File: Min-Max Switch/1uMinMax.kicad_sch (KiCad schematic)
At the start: 47 parts, among them J1 PJ301M12, J2 PJ301M12, J3 PJ301M12, J4 PJ301M12, J5 PJ301M12, J6 PJ301M12, J7 PJ301M12, J8 PJ301M12, P1 CONN_01X03, U1 TL074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

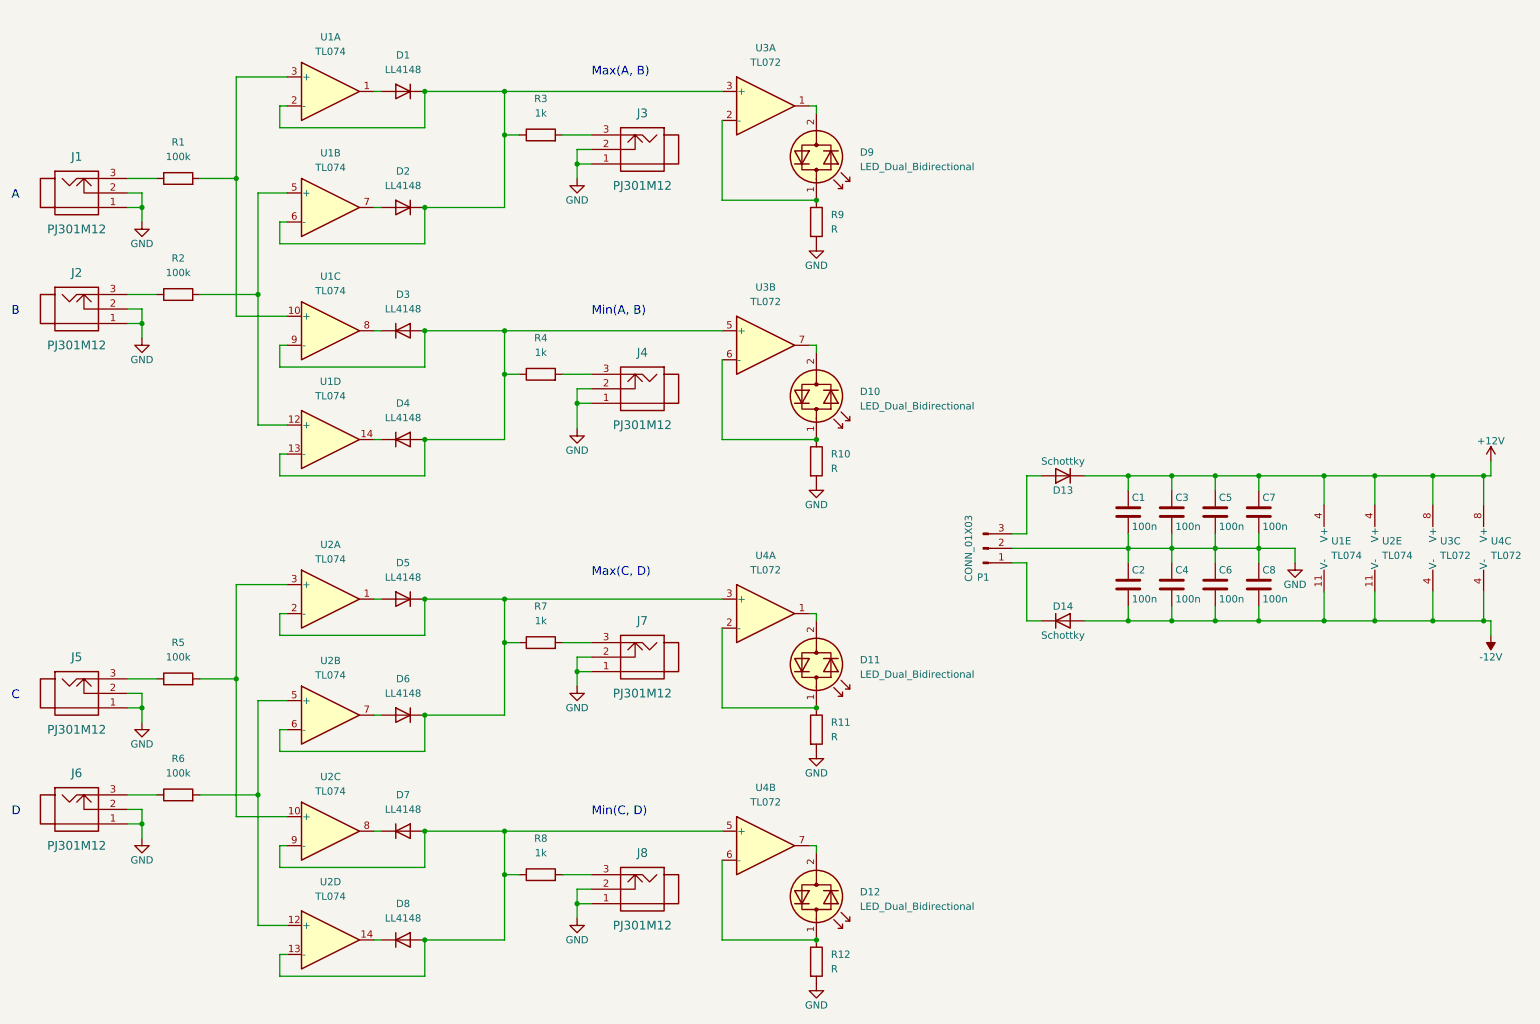
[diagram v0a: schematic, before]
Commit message: Updated sub-dom switch circuit. It now clones a section of the Mutable Instruments Kinks circuit
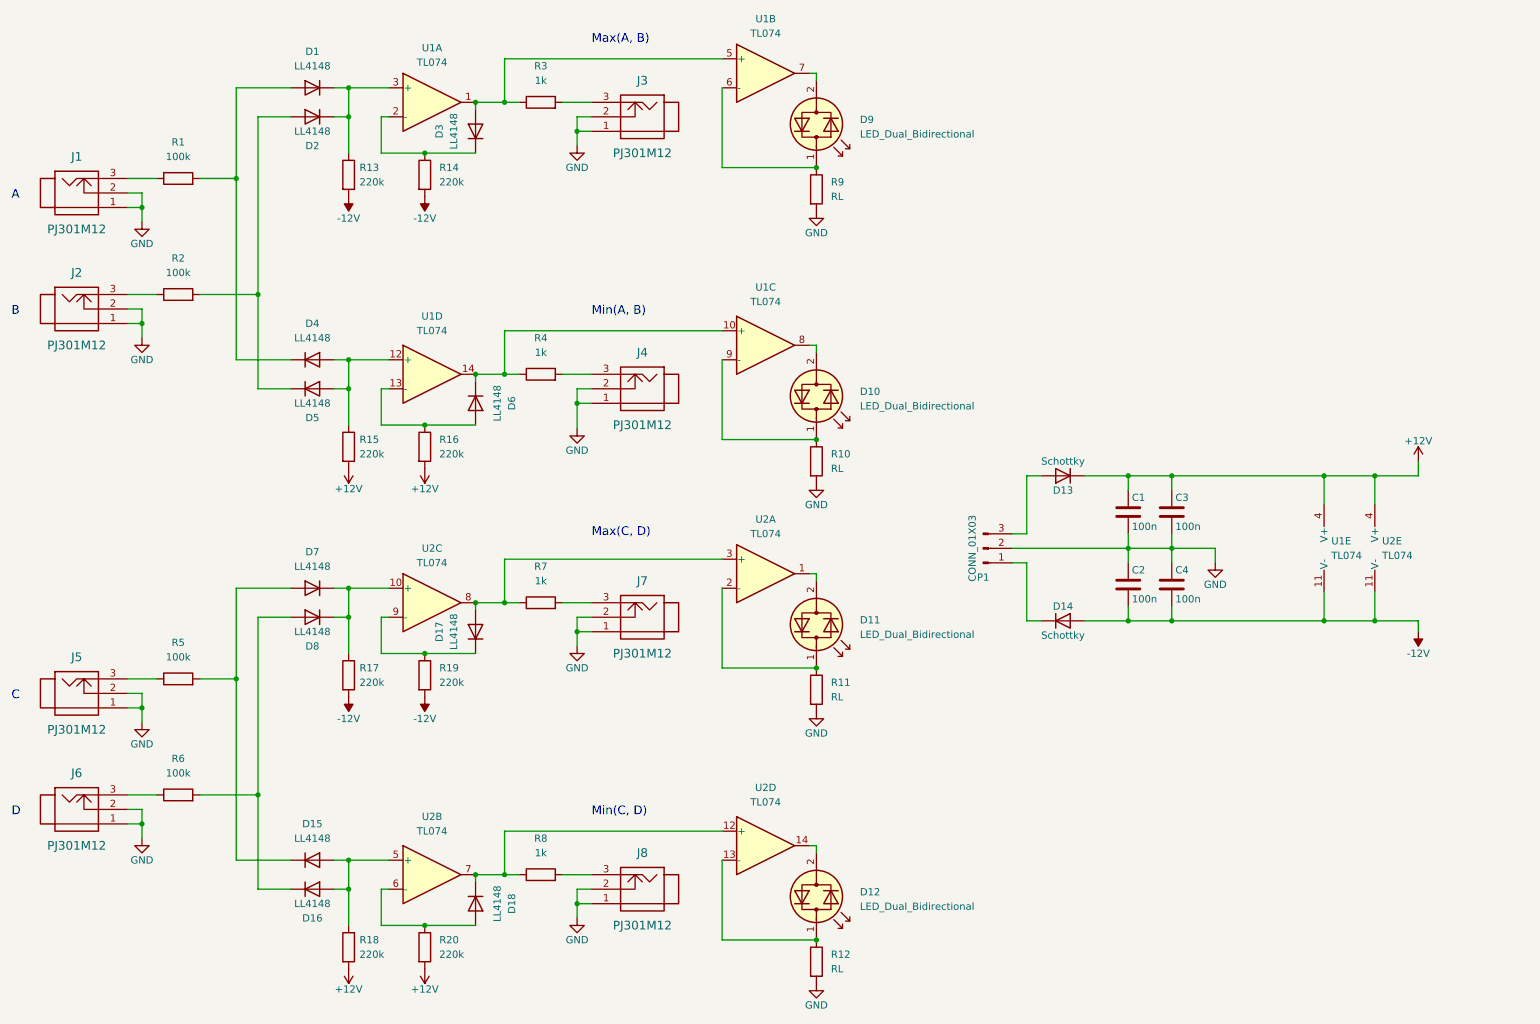
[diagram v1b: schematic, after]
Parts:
- removed C5, C6, C7, C8: 100n, Capacitor_SMD:C_0805_2012Metric_Pad1.18x1.45mm_HandSolder, symbol Device:C
- removed U3, U4: TL072, Package_SO:SOIC-8_3.9x4.9mm_P1.27mm, symbol Amplifier_Operational:TL072
- added D15, D16, D17, D18: LL4148, Diode_SMD:D_SOD-323_HandSoldering, symbol Diode:LL4148
- added R13, R14, R15, R16, R17, R18, R19, R20: 220k, Resistor_SMD:R_0805_2012Metric_Pad1.20x1.40mm_HandSolder, symbol Device:R
- R10, R11, R12, R9: value R -> RL
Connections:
- net +12V: now also R15.2, R16.2, R18.2, R20.2
- net -12V: now also R13.2, R14.2, R17.2, R19.2
- net at D11.1 (KA), R11.1: now also U2.2 (-)
- net at D11.2 (AK): now also U2.1
- net at D9.2 (AK): now also U1.7
- net at D9.1 (KA), R9.1: now also U1.6 (-)
- net at D10.1 (KA), R10.1: now also U1.9 (-)
- net at D10.2 (AK): now also U1.8
- net at D12.1 (KA), R12.1: now also U2.13 (-)
- net at D12.2 (AK): now also U2.14
- net at D8.1 (K): now also D7.1 (K), U2.10 (+), R17.1; no longer U2.14
- net at U1.1: now also D3.2 (A), R3.1, U1.5 (+); no longer D1.2 (A)
- net at U2.7: now also R8.1, U2.12 (+), D18.1 (K); no longer D6.2 (A)
- net at D2.2 (A): now also D5.1 (K), R2.2; no longer U1.7
- net at D3.1 (K): now also U1.2 (-), R14.1; no longer U1.8
- net at D4.1 (K): now also D1.2 (A), R1.2; no longer U1.14
- net at U2.8: now also R7.1, U2.3 (+), D17.2 (A); no longer D7.1 (K)
- net at D5.2 (A): now also D4.2 (A), U1.12 (+), R15.1; no longer U2.1
- new net: D17.1 (K), R19.1, U2.9 (-)
- new net: D18.2 (A), R20.1, U2.6 (-)
- new net: D16.1 (K), D8.2 (A), R6.2
- new net: D15.2 (A), D16.2 (A), R18.1, U2.5 (+)
- new net: D1.1 (K), D2.1 (K), R13.1, U1.3 (+)
- new net: D6.2 (A), R16.1, U1.13 (-)
- new net: D6.1 (K), R4.1, U1.10 (+), U1.14
- new net: D15.1 (K), D7.2 (A), R5.2
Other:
- moved on the sheet: D1, D11, D2, D3, D9, J3, J7, R11, R3, R7, R9, U1A
